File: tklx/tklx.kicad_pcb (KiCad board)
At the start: 2 copper layers, 400.1 x 128.6 mm, 244 parts, among them J1 USB_C_Receptacle_USB2.0_14P, J2 Conn_01x04, SW1 SW_Push, SW2 SW_Push, U1 ESP32-S2, U2 XC6206PxxxMR, U3 SRV05-4

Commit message: intial stm32 design
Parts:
- D106, D107, D108, D109, D110, D111, D112, D113, D114: moved to B.Cu
- moved D114 291.9 mm to (361.9, 123.8), turned to 90 degrees
- moved D113 273.9 mm to (342.9, 123.8), turned to 90 degrees
- moved D112 256.2 mm to (323.9, 123.8), turned to 90 degrees
- moved D111 238.6 mm to (304.8, 123.8), turned to 90 degrees
- moved D110 162.9 mm to (223.8, 123.8), turned to 90 degrees
- moved D109 141.8 mm to (200.0, 123.8), turned to 90 degrees
- moved D108 126.0 mm to (181.0, 123.8), turned to 90 degrees
- moved D107 111.4 mm to (161.9, 123.8), turned to 90 degrees
- moved D106 94.9 mm to (138.1, 123.8), turned to 90 degrees
- turned MX72 to 0 degrees
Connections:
- D114 pad 1: Net-(D114-K) -> ROW0
- D68 pad 2: Net-(D114-K) -> Net-(D68-A)
- MX68 pad 2: Net-(D114-K) -> Net-(D68-A)
- MX72 pad 1: COL2 -> unconnected-(MX72-COL-Pad1)

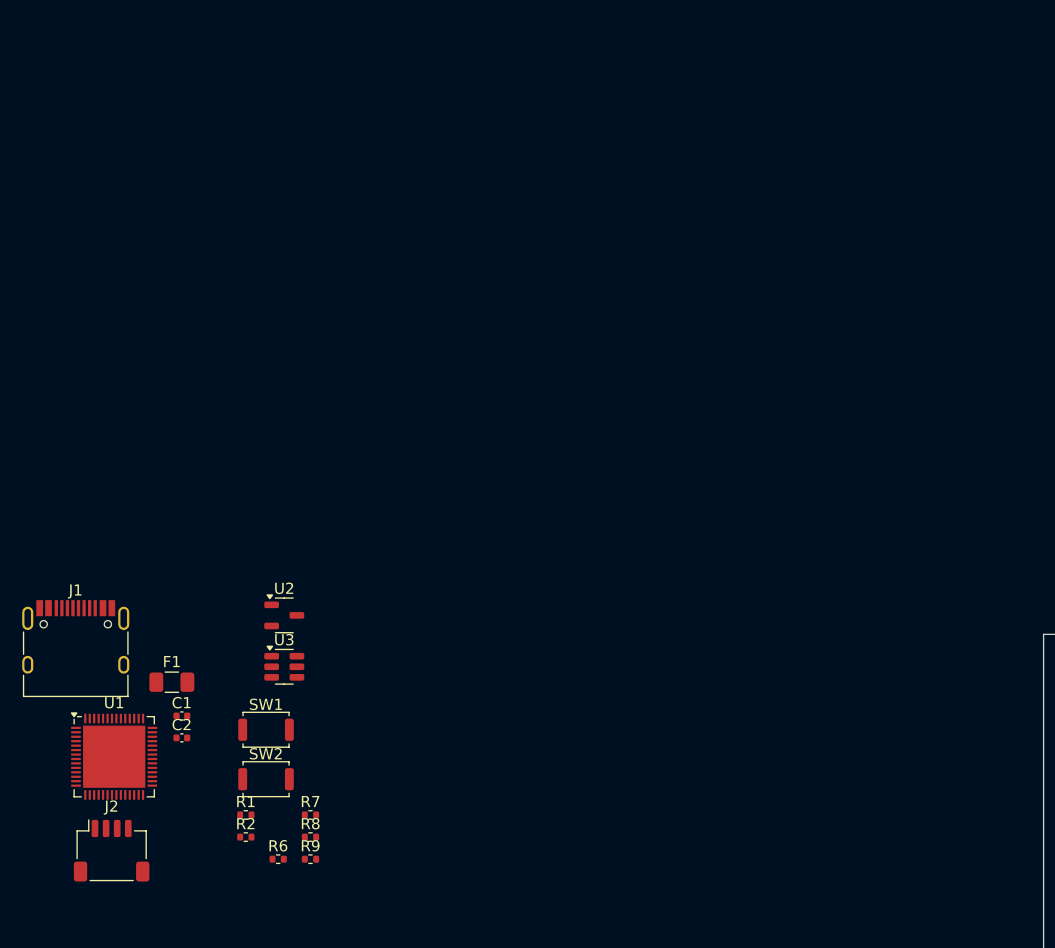
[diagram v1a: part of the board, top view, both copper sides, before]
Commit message: finished esp32 wireless design
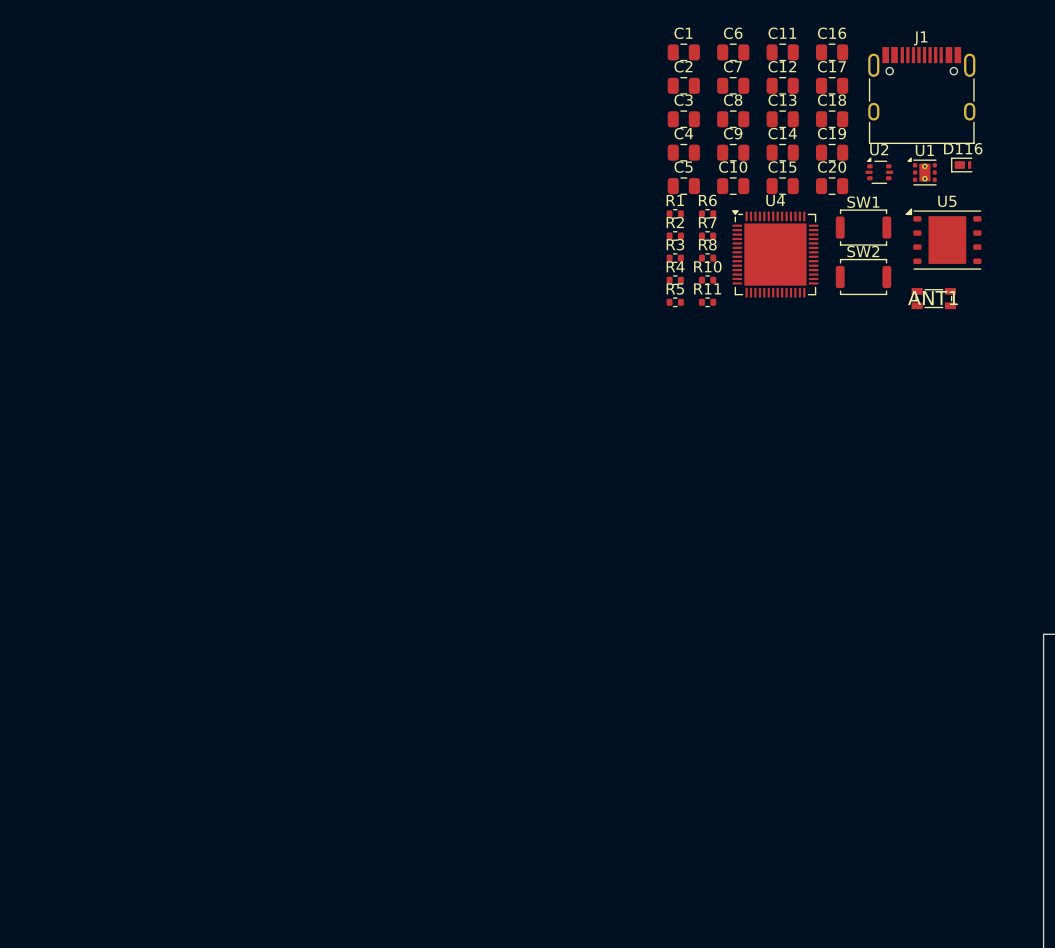
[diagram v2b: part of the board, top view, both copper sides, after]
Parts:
- removed F1: Fuse_Small, Fuse:Fuse_1206_3216Metric
- removed J2: Conn_01x04, Connector_JST:JST_SH_SM04B-SRSS-TB_1x04-1MP_P1.00mm_Horizontal
- removed R9: 5.1k, Resistor_SMD:R_0402_1005Metric
- removed U3: SRV05-4, Package_TO_SOT_SMD:SOT-23-6
- added ANT1: 2450AT18D0100E, Samacsys:2450AT18D0100E, F.Cu at (42.5, 74.6)
- added C10: 1uF, Capacitor_SMD:C_0805_2012Metric, F.Cu at (24.4, 64.4)
- added C11: 0.1uF, Capacitor_SMD:C_0805_2012Metric, F.Cu at (28.9, 52.4)
- added C12: 0.1uF, Capacitor_SMD:C_0805_2012Metric, F.Cu at (28.9, 55.4)
- added C13: 1uF, Capacitor_SMD:C_0805_2012Metric, F.Cu at (28.9, 58.4)
- added C14: 0.1uF, Capacitor_SMD:C_0805_2012Metric, F.Cu at (28.9, 61.4)
- added C15: 12pF, Capacitor_SMD:C_0805_2012Metric, F.Cu at (28.9, 64.4)
- added C16: 12pF, Capacitor_SMD:C_0805_2012Metric, F.Cu at (33.4, 52.4)
- added C17: NC, Capacitor_SMD:C_0805_2012Metric, F.Cu at (33.4, 55.4)
- added C18: NC, Capacitor_SMD:C_0805_2012Metric, F.Cu at (33.4, 58.4)
- added C19: 2.4pF, Capacitor_SMD:C_0805_2012Metric, F.Cu at (33.4, 61.4)
- added C20: 2.7pF, Capacitor_SMD:C_0805_2012Metric, F.Cu at (33.4, 64.4)
- added C3: 10uF, Capacitor_SMD:C_0805_2012Metric, F.Cu at (20.0, 58.4)
- added C4: 1uF, Capacitor_SMD:C_0805_2012Metric, F.Cu at (20.0, 61.4)
- added C5: 0.1uF, Capacitor_SMD:C_0805_2012Metric, F.Cu at (20.0, 64.4)
- added C6: 0.1uF, Capacitor_SMD:C_0805_2012Metric, F.Cu at (24.4, 52.4)
- added C7: 10nF, Capacitor_SMD:C_0805_2012Metric, F.Cu at (24.4, 55.4)
- added C8: 1uF, Capacitor_SMD:C_0805_2012Metric, F.Cu at (24.4, 58.4)
- added C9: 0.1uF, Capacitor_SMD:C_0805_2012Metric, F.Cu at (24.4, 61.4)
- added D116: PTVS5V0Z1USKP, Diode_SMD:Nexperia_DSN1608-2_1.6x0.8mm, F.Cu at (45.1, 62.5)
- added R10: 22, Resistor_SMD:R_0402_1005Metric, F.Cu at (22.1, 72.9)
- added R11: 0, Resistor_SMD:R_0402_1005Metric, F.Cu at (22.1, 74.9)
- added R3: 0, Resistor_SMD:R_0402_1005Metric, F.Cu at (19.2, 70.9)
- added R4: 0, Resistor_SMD:R_0402_1005Metric, F.Cu at (19.2, 72.9)
- added R5: 0, Resistor_SMD:R_0402_1005Metric, F.Cu at (19.2, 74.9)
- added U4: ESP32-S3, Package_DFN_QFN:QFN-56-1EP_7x7mm_P0.4mm_EP5.6x5.6mm, F.Cu at (28.2, 70.6)
- added U5: W25Q128JVP, Package_SON:WSON-8-1EP_6x5mm_P1.27mm_EP3.4x4.3mm, F.Cu at (43.7, 69.3)
- C1: value 1u -> 1uF; footprint Capacitor_SMD:C_0402_1005Metric -> Capacitor_SMD:C_0805_2012Metric
- C2: value 1u -> 2.2uF; footprint Capacitor_SMD:C_0402_1005Metric -> Capacitor_SMD:C_0805_2012Metric
- R6: value 5.1k -> 10k
- R7: value 1K -> 0
- R8: value 5.1k -> 0
- SW2: value SW_Push -> SW_SPST
- U1: value ESP32-S2 -> TLV76733DRVx; footprint Package_DFN_QFN:QFN-56-1EP_7x7mm_P0.4mm_EP5.6x5.6mm -> Package_SON:WSON-6-1EP_2x2mm_P0.65mm_EP1x1.6mm_ThermalVias
- U2: value XC6206PxxxMR -> USBLC6-2P6; footprint Package_TO_SOT_SMD:SOT-23-3 -> Package_TO_SOT_SMD:SOT-666
- moved J1 91.0 mm to (41.4, 56.7)
- moved U1 90.0 mm to (41.7, 63.2)
- moved C1 74.9 mm to (20.0, 52.4)
- moved C2 74.1 mm to (20.0, 55.4)
- moved SW1 70.3 mm to (36.2, 68.2)
- moved SW2 70.3 mm to (36.2, 72.6)
- moved R6 69.8 mm to (22.1, 66.9)
- moved U2 66.8 mm to (37.6, 63.2)
- moved R1 66.5 mm to (19.2, 66.9)
- moved R2 66.5 mm to (19.2, 68.9)
- moved R8 63.2 mm to (22.1, 70.9)
- moved R7 63.2 mm to (22.1, 68.9)
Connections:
- net RESET renamed /RESET
- C1 pad 1: +5V -> /VIN
- J1 pad A4: VBUS -> /VBUS
- J1 pad A6: D+ -> /D+
- J1 pad A7: D- -> /D-
- J1 pad A9: VBUS -> /VBUS
- J1 pad B4: VBUS -> /VBUS
- J1 pad B6: D+ -> /D+
- J1 pad B7: D- -> /D-
- J1 pad B9: VBUS -> /VBUS
- J1 pad S1: GND -> unconnected-(J1-SHIELD-PadS1)
- R7 pad 1: Q_SEL -> /SPIQ
- R7 pad 2: Net-(R7-Pad2) -> Net-(U4-SPIQ/GPIO31)
- R8 pad 2: Q_SEL -> /SPID
- SW2 pad 1: GND -> /BOOT
- SW2 pad 2: Net-(R7-Pad2) -> GND
- U1 pad 1: Net-(U1-VDDA-Pad1) -> +3V3
- U1 pad 2: unconnected-(U1-LNA_IN/RF-Pad2) -> +3V3
- U1 pad 3: Net-(U1-VDD3P3-Pad3) -> GND
- U1 pad 4: Net-(U1-VDD3P3-Pad3) -> /VIN
- U1 pad 5: unconnected-(U1-GPIO0/BOOT-Pad5) -> GND
- U1 pad 6: unconnected-(U1-GPIO1/ADC1_CH0-Pad6) -> /VIN
- U1 pad 7: unconnected-(U1-GPIO2/ADC1_CH1-Pad7) -> GND
- U2 pad 1: GND -> /D_N
- U2 pad 2: +3V3 -> GND
- U2 pad 3: +5V -> /D_P

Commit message: prelim esp32-mini design
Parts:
- removed ANT1: 2450AT18D0100E, Samacsys:2450AT18D0100E
- removed C10, C13, C8: 1uF, Capacitor_SMD:C_0805_2012Metric
- removed C11, C12, C14, C9: 0.1uF, Capacitor_SMD:C_0805_2012Metric
- removed C15, C16: 12pF, Capacitor_SMD:C_0805_2012Metric
- removed C17, C18: NC, Capacitor_SMD:C_0805_2012Metric
- removed C19: 2.4pF, Capacitor_SMD:C_0805_2012Metric
- removed C20: 2.7pF, Capacitor_SMD:C_0805_2012Metric
- removed C7: 10nF, Capacitor_SMD:C_0805_2012Metric
- removed D116: PTVS5V0Z1USKP, Diode_SMD:Nexperia_DSN1608-2_1.6x0.8mm
- removed R10: 22, Resistor_SMD:R_0402_1005Metric
- removed R11, R3, R4, R5, R7, R8: 0, Resistor_SMD:R_0402_1005Metric
- removed R6: 10k, Resistor_SMD:R_0402_1005Metric
- removed U2: USBLC6-2P6, Package_TO_SOT_SMD:SOT-666
- removed U4: ESP32-S3, Package_DFN_QFN:QFN-56-1EP_7x7mm_P0.4mm_EP5.6x5.6mm
- removed U5: W25Q128JVP, Package_SON:WSON-8-1EP_6x5mm_P1.27mm_EP3.4x4.3mm
- added U3: ESP32-S3-MINI-1, RF_Module:ESP32-S2-MINI-1, B.Cu at (77.0, 118.2)
- C1: value 1uF -> 10uF; moved to B.Cu
- C2: value 2.2uF -> 10uF; moved to B.Cu
- C3: value 10uF -> 100nF; moved to B.Cu
- C4: value 1uF -> 22uF; moved to B.Cu
- C5: value 0.1uF -> 1uF; moved to B.Cu
- C6: value 0.1uF -> 100nF; moved to B.Cu
- J1: value USB_C_Receptacle_USB2.0_14P -> Conn_01x04; footprint Connector_USB:USB_C_Receptacle_HRO_TYPE-C-31-M-12 -> Connector_JST:JST_EH_S4B-EH_1x04_P2.50mm_Horizontal; moved to B.Cu
- R1: value 5.1k -> 10k; footprint Resistor_SMD:R_0402_1005Metric -> Resistor_SMD:R_0805_2012Metric; moved to B.Cu
- R2: value 5.1k -> 100; footprint Resistor_SMD:R_0402_1005Metric -> Resistor_SMD:R_0805_2012Metric; moved to B.Cu
- SW1: footprint Button_Switch_SMD:SW_Push_SPST_NO_Alps_SKRK -> Button_Switch_SMD:SW_Push_1P1T_XKB_TS-1187A; moved to B.Cu
- SW2: value SW_SPST -> SW_Push; footprint Button_Switch_SMD:SW_Push_SPST_NO_Alps_SKRK -> Button_Switch_SMD:SW_Push_1P1T_XKB_TS-1187A; moved to B.Cu
- U1: value TLV76733DRVx -> AMS1117-3.3; footprint Package_SON:WSON-6-1EP_2x2mm_P0.65mm_EP1x1.6mm_ThermalVias -> Package_TO_SOT_SMD:SOT-223-3_TabPin2; moved to B.Cu
- moved C2 88.8 mm to (67.7, 130.3)
- moved R2 86.2 mm to (87.3, 121.8)
- moved J1 84.1 mm to (89.7, 125.6)
- moved C6 84.1 mm to (67.2, 124.8), turned to -90 degrees
- moved C1 78.8 mm to (66.7, 115.8), turned to -90 degrees
- moved C3 75.3 mm to (55.4, 124.9), turned to 90 degrees
- moved C4 74.7 mm to (66.7, 119.8), turned to -90 degrees
- moved SW2 71.3 mm to (91.7, 117.3)
- moved U1 65.6 mm to (61.1, 125.8), turned to 180 degrees
- moved C5 64.8 mm to (55.1, 118.8)
- moved R1 60.3 mm to (55.1, 115.3), turned to 180 degrees
- moved SW1 54.8 mm to (61.1, 117.0), turned to 180 degrees
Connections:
- C1 pad 1: /VIN -> EN
- C2 pad 1: +3V3 -> +5V
- C3 pad 1: +3V3 -> EN
- C4 pad 1: +3V3 -> EN
- C5 pad 1: +3V3 -> Net-(C5-Pad1)
- C6 pad 1: VDD3P3 -> GND
- C6 pad 2: GND -> EN
- R1 pad 1: Net-(J1-CC2) -> EN
- R1 pad 2: GND -> Net-(C5-Pad1)
- R2 pad 1: Net-(J1-CC1) -> BOOT
- R2 pad 2: GND -> Net-(R2-Pad2)
- SW1 pad 1: GND -> EN
- SW1 pad 2: /RESET -> GND
- SW2 pad 1: /BOOT -> Net-(R2-Pad2)
- U1 pad 1: +3V3 -> GND
- U1 pad 2: +3V3 -> EN
- U1 pad 3: GND -> +5V
